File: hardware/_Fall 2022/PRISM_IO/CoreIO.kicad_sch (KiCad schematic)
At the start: 21 parts, among them J1 Conn_01x07_Female, Q1 Q_NJFET_DGS, Q2 Q_NJFET_DGS, SW1 SW_SPST, SW2 SW_SPST, U1 XT30UPB-M, U2 XT30UPB-M

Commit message: work on PRISM io
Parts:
- removed J1: Conn_01x07_Female, symbol Connector:Conn_01x07_Female
- removed SW1, SW2: SW_SPST, symbol Switch:SW_SPST
- added J1: CORE_FC, Connector_JST:JST_PH_S7B-PH-K_1x07_P2.00mm_Horizontal, symbol Connector_Generic:Conn_01x07
- added J2: COTS_SWITCH_PLUG, Connector_JST:JST_PH_S2B-PH-K_1x02_P2.00mm_Horizontal, symbol Connector:Conn_01x02_Female
- added S1, S2: D2F-01F, SW_D2F-01F, symbol omron_D2F:D2F-01F
- added S3: COTS_SWITCH, SW_D2F-01F, symbol omron_D2F:D2F-01F
- BT1, BT2: footprint (none) -> JST:JST_SFH_SM02B-SFHRS-TF_02x1.80mm_Angled
- D1: footprint (none) -> LED_SMD:LED_0603_1608Metric
- D2, D5: footprint (none) -> Diode_THT:D_5KPW_P12.70mm_Horizontal
- R1, R10, R11, R2, R5, R6, R7, R8, R9: footprint (none) -> Resistor_SMD:R_0201_0603Metric
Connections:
- net ARM: now also J1.1 (Pin_1)
- net CONT 1: now also J1.3 (Pin_3)
- net CONT 2: now also J1.2 (Pin_2)
- net GND: now also J1.7 (Pin_7)
- net PYRO 1: now also J1.5 (Pin_5)
- net PYRO 2: now also J1.4 (Pin_4)
- net VBAT: now reaches D1.2 (A)
- net VBAT: now also J1.6 (Pin_6), S1.3, S2.1
- net Switch1IN renamed SWITCH1
- net SWITCH1: now also S1.1
- new net: J2.2 (Pin_2), S3.1
- new net: J2.1 (Pin_1), S3.3
- no-connect marks 0 -> 3
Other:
- note added: "ARM SWITCH"
- note added: "BATTERY"
- note added: "COTS SWITCH"
- note added: "FC HEADER"
- note added: "MASTER SWITCH"
- note added: "PYRO 1"
- note added: "PYRO 2"
- note added: "Voltage divider to read vbat"
- note removed: "ARMING SWITCH"
- note removed: "Arming Safe Switch"
- note removed: "Master Power Switch"
- note removed: "POWER SWITCH"
- note removed: "Power Multiplexer"
- note removed: "Reverse Current Protection"
- note removed: "TO CORE1"
- note removed: "Terminals to Electromechanical Arming Switch"
- moved on the sheet: BT1, BT2, D1, D2, D5, Q1, Q2, R1, R10, R11, R2, R5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

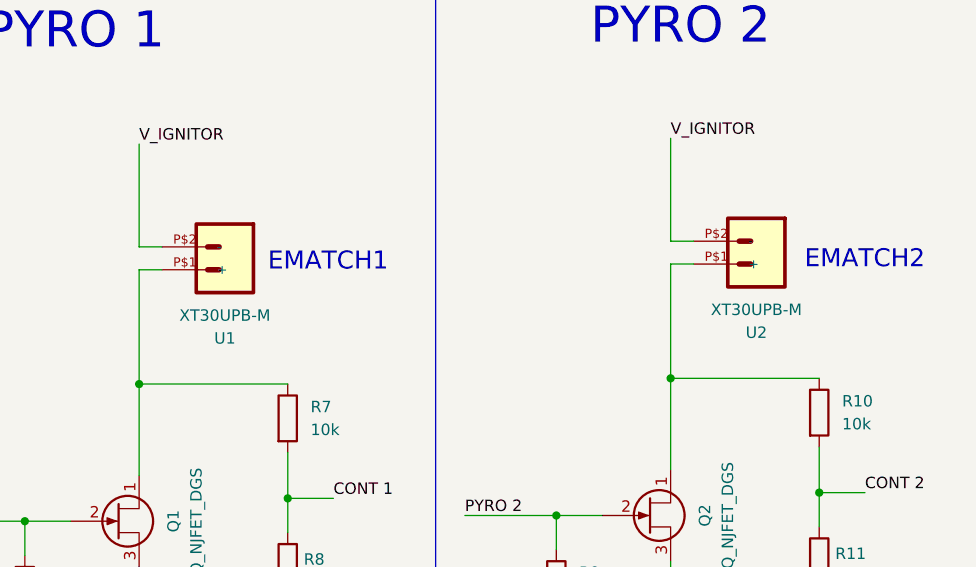
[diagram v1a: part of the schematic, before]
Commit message: fixed some footprints on PRISM IO
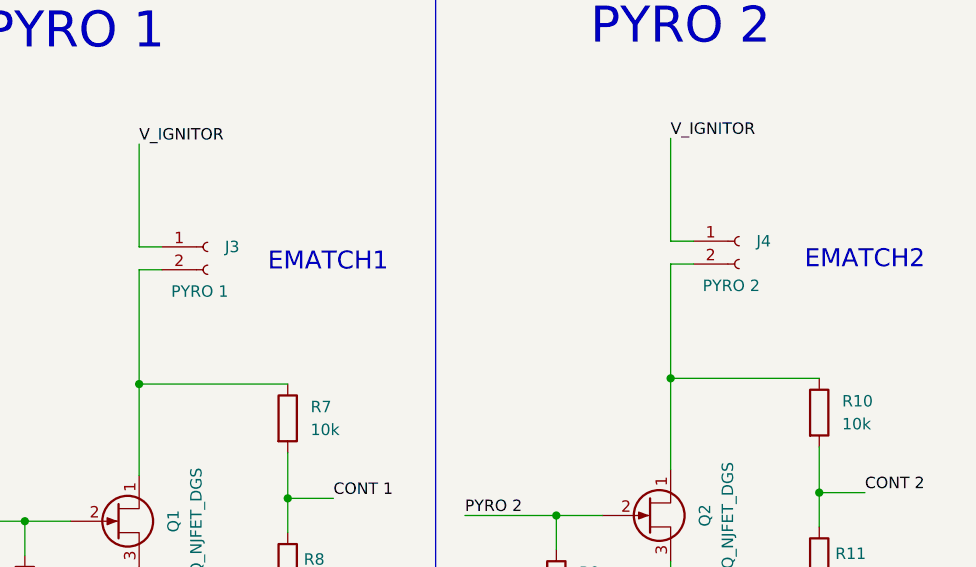
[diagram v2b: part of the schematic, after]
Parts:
- removed U1, U2: XT30UPB-M, XT30UPB-M, symbol XT30:XT30UPB-M
- added J3: PYRO 1, JST:JST_SFH_SM02B-SFHRS-TF_02x1.80mm_Angled, symbol Connector:Conn_01x02_Female
- added J4: PYRO 2, JST:JST_SFH_SM02B-SFHRS-TF_02x1.80mm_Angled, symbol Connector:Conn_01x02_Female
- D2, D5: footprint Diode_THT:D_5KPW_P12.70mm_Horizontal -> Diode_SMD:D_0201_0603Metric
- S1, S2, S3: footprint SW_D2F-01F -> Sensors:SW_D2F-01F
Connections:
- net V_IGNITOR: now also J3.1 (Pin_1), J4.1 (Pin_1)
- net at Q2.1 (D), R10.1: now also J4.2 (Pin_2)
- net at Q1.1 (D), R7.1: now also J3.2 (Pin_2)
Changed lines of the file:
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@@
     (property "Reference" "D5" (id 0) (at 83.439 48.895 0))
     (property "Value" "D_Schottky" (id 1) (at 83.439 50.546 0))
-    (property "Footprint" "Diode_THT:D_5KPW_P12.70mm_Horizontal" (id 2) (at 83.439 52.832 0)
+    (property "Footprint" "Diode_SMD:D_0201_0603Metric" (id 2) (at 83.439 52.832 0)
       (effects (font (size 1.27 1.27)) hide)
     )
@@
     (property "Reference" "S3" (id 0) (at 260.604 31.6484 0))
     (property "Value" "COTS_SWITCH" (id 1) (at 260.604 34.1884 0))
-    (property "Footprint" "SW_D2F-01F" (id 2) (at 260.604 39.37 0)
+    (property "Footprint" "Sensors:SW_D2F-01F" (id 2) (at 260.604 39.37 0)
       (effects (font (size 1.27 1.27)) (justify bottom) hide)
     )
@@
     (property "Reference" "D2" (id 0) (at 83.439 25.9111 0))
     (property "Value" "D_Schottky" (id 1) (at 83.439 28.448 0))
-    (property "Footprint" "Diode_THT:D_5KPW_P12.70mm_Horizontal" (id 2) (at 83.439 31.496 0)
+    (property "Footprint" "Diode_SMD:D_0201_0603Metric" (id 2) (at 83.439 31.496 0)
       (effects (font (size 1.27 1.27)) hide)
     )
     (property "Datasheet" "~" (id 3) (at 83.439 31.496 0)
+      (effects (font (size 1.27 1.27)) hide)
+    )
+    (pin "1")
+    (pin "2")
+  )
+  (symbol (lib_id "Connector:Conn_01x02_Female") (at 108.204 102.743 0) (unit 1)
+    (in_bom yes) (on_board yes)
+    (property "Reference" "J4" (id 0) (at 110.109 102.7429 0)
+      (effects (font (size 1.27 1.27)) (justify left))
+    )
+    (property "Value" "PYRO 2" (id 1) (at 104.14 107.696 0)
+      (effects (font (size 1.27 1.27)) (justify left))
+    )
+    (property "Footprint" "JST:JST_SFH_SM02B-SFHRS-TF_02x1.80mm_Angled" (id 2) (at 108.204 102.743 0)
+      (effects (font (size 1.27 1.27)) hide)
+    )
+    (property "Datasheet" "~" (id 3) (at 108.204 102.743 0)
       (effects (font (size 1.27 1.27)) hide)
     )
@@
     (pin "3")
   )
-  (symbol (lib_id "XT30:XT30UPB-M") (at 110.744 102.743 180) (unit 1)
-    (in_bom yes) (on_board yes)
-    (property "Reference" "U2" (id 0) (at 110.109 112.903 0))
-    (property "Value" "XT30UPB-M" (id 1) (at 110.109 110.363 0))
-    (property "Footprint" "XT30UPB-M" (id 2) (at 110.744 102.743 0)
-      (effects (font (size 1.27 1.27)) (justify left bottom) hide)
-    )
-    (property "Datasheet" "" (id 3) (at 110.744 102.743 0)
-      (effects (font (size 1.27 1.27)) (justify left bottom) hide)
-    )
-    (pin "P$1")
-    (pin "P$2")
-  )
   (symbol (lib_id "power:GND") (at 117.094 145.923 0) (unit 1)
     (in_bom yes) (on_board yes) (fields_autoplaced)
@@
     (pin "1")
   )
-  (symbol (lib_id "XT30:XT30UPB-M") (at 51.689 103.378 180) (unit 1)
-    (in_bom yes) (on_board yes)
-    (property "Reference" "U1" (id 0) (at 51.054 113.538 0))
-    (property "Value" "XT30UPB-M" (id 1) (at 51.054 110.998 0))
-    (property "Footprint" "XT30UPB-M" (id 2) (at 51.689 103.378 0)
-      (effects (font (size 1.27 1.27)) (justify left bottom) hide)
-    )
-    (property "Datasheet" "" (id 3) (at 51.689 103.378 0)
-      (effects (font (size 1.27 1.27)) (justify left bottom) hide)
-    )
-    (pin "P$1")
-    (pin "P$2")
-  )
   (symbol (lib_id "Device:Battery_Cell") (at 79.629 59.182 0) (unit 1)
     (in_bom yes) (on_board yes)
@@
     (property "Reference" "S2" (id 0) (at 203.9112 24.8412 0))
     (property "Value" "D2F-01F" (id 1) (at 203.9112 27.3812 0))
-    (property "Footprint" "SW_D2F-01F" (id 2) (at 203.9112 32.4612 0)
+    (property "Footprint" "Sensors:SW_D2F-01F" (id 2) (at 203.9112 32.4612 0)
       (effects (font (size 1.27 1.27)) (justify bottom) hide)
     )
@@
     )
     (property "Datasheet" "~" (id 3) (at 79.629 36.322 90)
+      (effects (font (size 1.27 1.27)) hide)
+    )
+    (pin "1")
+    (pin "2")
+  )
+  (symbol (lib_id "Connector:Conn_01x02_Female") (at 49.149 103.378 0) (unit 1)
+    (in_bom yes) (on_board yes)
+    (property "Reference" "J3" (id 0) (at 51.054 103.3779 0)
+      (effects (font (size 1.27 1.27)) (justify left))
+    )
+    (property "Value" "PYRO 1" (id 1) (at 45.085 108.331 0)
+      (effects (font (size 1.27 1.27)) (justify left))
+    )
+    (property "Footprint" "JST:JST_SFH_SM02B-SFHRS-TF_02x1.80mm_Angled" (id 2) (at 49.149 103.378 0)
+      (effects (font (size 1.27 1.27)) hide)
+    )
+    (property "Datasheet" "~" (id 3) (at 49.149 103.378 0)
       (effects (font (size 1.27 1.27)) hide)
     )
@@
     (property "Reference" "S1" (id 0) (at 143.002 31.242 0))
     (property "Value" "D2F-01F" (id 1) (at 143.002 33.782 0))
-    (property "Footprint" "SW_D2F-01F" (id 2) (at 143.002 38.862 0)
+    (property "Footprint" "Sensors:SW_D2F-01F" (id 2) (at 143.002 38.862 0)
       (effects (font (size 1.27 1.27)) (justify bottom) hide)
     )
@@
     )
     (path "/35372d0b-4634-4a41-8574-bc3ec858fb57"
-      (reference "D2") (unit 1) (value "D_Schottky") (footprint "Diode_THT:D_5KPW_P12.70mm_Horizontal")
+      (reference "D2") (unit 1) (value "D_Schottky") (footprint "Diode_SMD:D_0201_0603Metric")
     )
     (path "/1aaf8365-07c5-4cef-9f43-16a4a8dc5838"
-      (reference "D5") (unit 1) (value "D_Schottky") (footprint "Diode_THT:D_5KPW_P12.70mm_Horizontal")
+      (reference "D5") (unit 1) (value "D_Schottky") (footprint "Diode_SMD:D_0201_0603Metric")
     )
     (path "/64c13c00-b658-43ca-b50b-62021061db88"
@@
       (reference "J2") (unit 1) (value "COTS_SWITCH_PLUG") (footprint "Connector_JST:JST_PH_S2B-PH-K_1x02_P2.00mm_Horizontal")
     )
+    (path "/bb4cb2f2-6568-47a9-83a0-29db5cfe61cd"
+      (reference "J3") (unit 1) (value "PYRO 1") (footprint "JST:JST_SFH_SM02B-SFHRS-TF_02x1.80mm_Angled")
+    )
+    (path "/375b75fe-bffc-4fb5-be61-bc10a8d7dbec"
+      (reference "J4") (unit 1) (value "PYRO 2") (footprint "JST:JST_SFH_SM02B-SFHRS-TF_02x1.80mm_Angled")
+    )
     (path "/670b0083-9a1c-4c59-921e-85323bb58a9c"
       (reference "Q1") (unit 1) (value "Q_NJFET_DGS") (footprint "")
@@
     )
     (path "/d452f4af-993d-4b1c-8140-b8be4de7e9cc"
-      (reference "S1") (unit 1) (value "D2F-01F") (footprint "SW_D2F-01F")
+      (reference "S1") (unit 1) (value "D2F-01F") (footprint "Sensors:SW_D2F-01F")
     )
     (path "/8e3b84bb-e6a5-4499-b86c-167ffe69815e"
-      (reference "S2") (unit 1) (value "D2F-01F") (footprint "SW_D2F-01F")
+      (reference "S2") (unit 1) (value "D2F-01F") (footprint "Sensors:SW_D2F-01F")
     )
     (path "/34663a8d-3b19-42c4-b4c1-b3d184cb9217"
-      (reference "S3") (unit 1) (value "COTS_SWITCH") (footprint "SW_D2F-01F")
-    )
-    (path "/8515ef7b-0617-4b94-b91e-56d6d5b00154"
-      (reference "U1") (unit 1) (value "XT30UPB-M") (footprint "XT30UPB-M")
-    )
-    (path "/6a9a6943-ab1f-4fdb-8ac5-b492c69c1897"
-      (reference "U2") (unit 1) (value "XT30UPB-M") (footprint "XT30UPB-M")
-    )
-  )
+      (reference "S3") (unit 1) (value "COTS_SWITCH") (footprint "Sensors:SW_D2F-01F")
+    )
+  )

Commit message: add footprint for diode
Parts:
- removed D2, D5: D_Schottky, Diode_SMD:D_0201_0603Metric, symbol Device:D_Schottky
- added D2, D3: SS54, JLC_footprints:DO-214AC, symbol SS54:SS54
- added JP1, JP2, JP3: Jumper, Jumper:SolderJumper-3_P1.3mm_Open_Pad1.0x1.5mm_NumberLabels, symbol Jumper:SolderJumper_3_Open
- S1: value D2F-01F -> POWER
- S2: value D2F-01F -> ARM
- S3: value COTS_SWITCH -> COTS
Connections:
- net SWITCH1: now also D2.C, D3.C
- net VBAT: now also JP1.2 (C); no longer S1.3
- net V_IGNITOR: now also JP2.2 (C)
- net at BT2.1 (+): now also D3.A
- net at S3.2: now also JP3.1 (A)
- net at S3.3: now also JP3.3 (B); no longer J2.1 (Pin_1)
- net at BT1.1 (+): now also D2.A
- net at S2.2: now also JP2.1 (A)
- net at S2.3: now also JP2.3 (B)
- net at S1.2: now also JP1.1 (A)
- new net: J2.1 (Pin_1), JP3.2 (C)
- new net: JP1.3 (B), S1.3
- no-connect marks 3 -> 0
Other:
- moved on the sheet: BT1, BT2, D1, J2, R1, R2, R5, S1

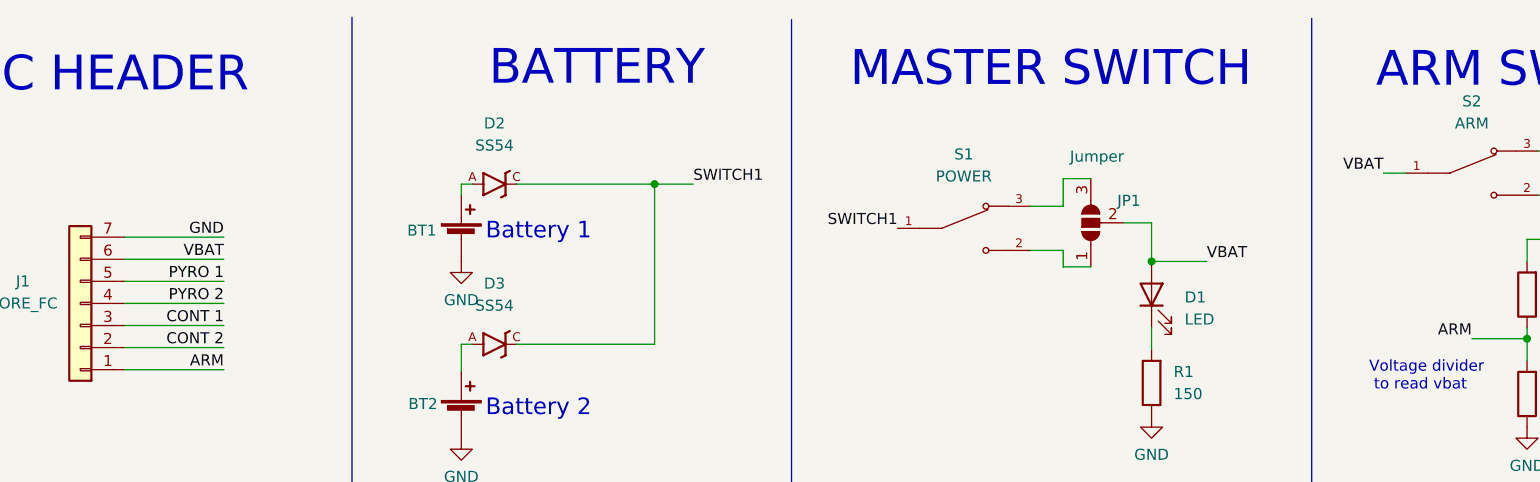
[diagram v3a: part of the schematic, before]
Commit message: Complete PRISM Teensy layout
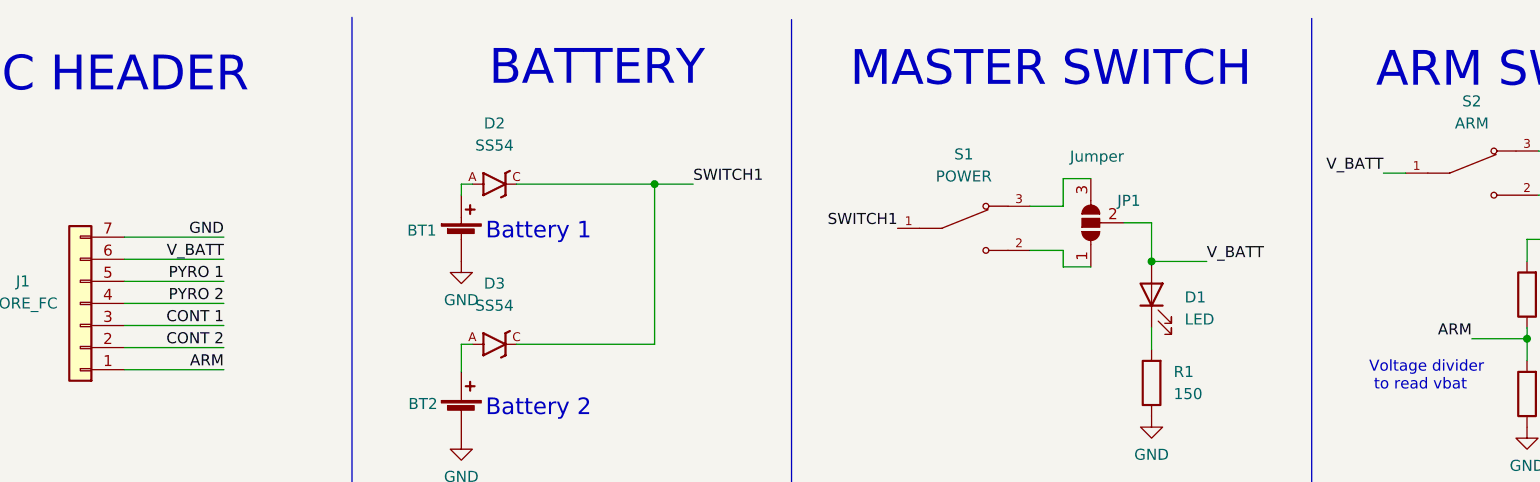
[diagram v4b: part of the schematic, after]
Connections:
- net VBAT renamed V_BATT
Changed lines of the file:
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@@
     (effects (font (size 1.27 1.27)) (justify left bottom))
   )
-  (label "VBAT" (at 165.735 40.005 0)
+  (label "V_BATT" (at 165.735 40.005 0)
     (effects (font (size 1.27 1.27)) (justify left bottom))
   )
@@
     (effects (font (size 1.27 1.27)) (justify right bottom))
   )
-  (label "VBAT" (at 186.055 29.845 180)
+  (label "V_BATT" (at 186.055 29.845 180)
     (effects (font (size 1.27 1.27)) (justify right bottom))
   )
@@
     (effects (font (size 1.27 1.27)) (justify right bottom))
   )
-  (label "VBAT" (at 52.705 39.751 180)
+  (label "V_BATT" (at 52.705 39.751 180)
     (effects (font (size 1.27 1.27)) (justify right bottom))
   )
